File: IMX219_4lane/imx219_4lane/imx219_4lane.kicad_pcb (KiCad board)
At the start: 4 copper layers, 25 x 24 mm, 26 parts, among them J1 DF37NC-30DS-0.4V, J2 FPC 28 pin connector, Q1 NTR5103N, Q2 NTR5103N, U1 AMPM, U2 LM3670MF, U3 AP7331, U4 AP7331

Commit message: zone concept
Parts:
- moved J2 1.50 mm to (32.5, 38.8)
- moved L1 1.00 mm to (26.5, 36.0)
- moved L2 1.00 mm to (28.0, 36.0)
- moved L3 1.00 mm to (31.0, 36.0)
- moved L4 1.00 mm to (32.5, 36.0)
- moved L5 1.00 mm to (29.5, 36.0)
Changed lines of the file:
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@@
 (kicad_pcb (version 20211014) (generator pcbnew)
   (general
-    (thickness 4.69)
+    (thickness 1.60252)
   )
   (paper "A4")
@@
       (layer "F.SilkS" (type "Top Silk Screen"))
       (layer "F.Paste" (type "Top Solder Paste"))
-      (layer "F.Mask" (type "Top Solder Mask") (thickness 0.01))
-      (layer "F.Cu" (type "copper") (thickness 0.035))
-      (layer "dielectric 1" (type "core") (thickness 1.51) (material "FR4") (epsilon_r 4.5) (loss_tangent 0.02))
+      (layer "F.Mask" (type "Top Solder Mask") (thickness 0.025))
+      (layer "F.Cu" (type "copper") (thickness 0.04))
+      (layer "dielectric 1" (type "core") (thickness 0.13626) (material "FR4") (epsilon_r 4.5) (loss_tangent 0.02))
       (layer "In1.Cu" (type "copper") (thickness 0.035))
-      (layer "dielectric 2" (type "prepreg") (thickness 1.51) (material "FR4") (epsilon_r 4.5) (loss_tangent 0.02))
+      (layer "dielectric 2" (type "prepreg") (thickness 1.13) (material "FR4") (epsilon_r 4.5) (loss_tangent 0.02))
       (layer "In2.Cu" (type "copper") (thickness 0.035))
-      (layer "dielectric 3" (type "core") (thickness 1.51) (material "FR4") (epsilon_r 4.5) (loss_tangent 0.02))
-      (layer "B.Cu" (type "copper") (thickness 0.035))
-      (layer "B.Mask" (type "Bottom Solder Mask") (thickness 0.01))
+      (layer "dielectric 3" (type "core") (thickness 0.13626) (material "FR4") (epsilon_r 4.5) (loss_tangent 0.02))
+      (layer "B.Cu" (type "copper") (thickness 0.04))
+      (layer "B.Mask" (type "Bottom Solder Mask") (thickness 0.025))
       (layer "B.Paste" (type "Bottom Solder Paste"))
       (layer "B.SilkS" (type "Bottom Silk Screen"))
@@
   (net 41 "GND")
   (footprint "unsurv_offline_pcb_footprints:Molex 505110-2891" (layer "F.Cu")
-    (at 32.5 37.25)
+    (at 32.5 38.75)
     (property "Sheetfile" "imx219_4lane.kicad_sch")
     (property "Sheetname" "")
@@
     (pad "30" smd roundrect (at 9.05 2.7) (size 2 1.3) (layers "F.Cu" "F.Paste" "F.Mask") (roundrect_rratio 0.25)
       (net 2 "SHELL") (pinfunction "Pin_30") (pintype "passive"))
+    (model "${KICAD6_3DMODEL_DIR}/imported/5051102891.stp"
+      (offset (xyz 0 -1 0))
+      (scale (xyz 1 1 1))
+      (rotate (xyz -90 0 0))
+    )
   )
   (footprint "Capacitor_SMD:C_0603_1608Metric" (layer "F.Cu")
@@
   )
   (footprint "unsurv_offline_pcb_footprints:DLP11SN900HL2L_hand_solder" (layer "F.Cu")
-    (at 28 35 -90)
+    (at 28 36 -90)
     (property "Sheetfile" "imx219_4lane.kicad_sch")
     (property "Sheetname" "")
@@
     (property "Sheetname" "")
     (attr smd)
-    (fp_text reference "Q2" (at -0.475 -3.375) (layer "F.SilkS")
+    (fp_text reference "Q2" (at -0.475 -4.375) (layer "F.SilkS")
       (effects (font (size 1 1) (thickness 0.15)))
     )
@@
   )
   (footprint "unsurv_offline_pcb_footprints:DLP11SN900HL2L_hand_solder" (layer "F.Cu")
-    (at 29.5 35 -90)
+    (at 29.5 36 -90)
     (property "Sheetfile" "imx219_4lane.kicad_sch")
     (property "Sheetname" "")
@@
   )
   (footprint "unsurv_offline_pcb_footprints:DLP11SN900HL2L_hand_solder" (layer "F.Cu")
-    (at 26.5 35 90)
+    (at 26.5 36 90)
     (property "Sheetfile" "imx219_4lane.kicad_sch")
     (property "Sheetname" "")
@@
   )
   (footprint "unsurv_offline_pcb_footprints:DLP11SN900HL2L_hand_solder" (layer "F.Cu")
-    (at 31 35 -90)
+    (at 31 36 -90)
     (property "Sheetfile" "imx219_4lane.kicad_sch")
     (property "Sheetname" "")
@@
   )
   (footprint "unsurv_offline_pcb_footprints:DLP11SN900HL2L_hand_solder" (layer "F.Cu")
-    (at 32.5 35 -90)
-    (property "Sheetfile" "imx219_4lane.kicad_sch")
-    (property "Sheetname" "")
+    (at 32.5 36 -90)
+    (property "Sheetfile" "imx219_4lane.kicad_sch")
+    (property "Sheetname" "")

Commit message: update
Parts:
- moved C5 9.43 mm to (40.2, 34.6)
- moved C6 9.43 mm to (34.2, 34.6)
- moved U3 9.43 mm to (37.2, 34.6)
- moved C10 8.54 mm to (37.5, 26.0)
- moved C9 8.54 mm to (43.5, 26.0)
- moved U4 8.54 mm to (40.5, 26.0)
- moved C2 8.34 mm to (34.2, 21.2), turned to 0 degrees
- moved C1 3.75 mm to (28.2, 22.5)
- moved C3 3.72 mm to (31.0, 21.2), turned to 180 degrees
- moved Q1 2.83 mm to (23.0, 26.5)
- moved Q2 2.83 mm to (23.0, 30.0)
- moved R1 2.83 mm to (26.0, 26.5)
- moved R2 2.83 mm to (26.0, 30.0)
- moved C7 2.75 mm to (43.8, 30.0)
- moved C8 2.75 mm to (35.8, 30.0)
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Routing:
- net GND: track 0.00 -> 21.9 mm, vias 0 -> 20
- net +5V: track 0.00 -> 16.8 mm, vias 0 -> 8
- net +1V8: track 0.00 -> 4.67 mm, vias 0 -> 1
- net +1V2: track 0.00 -> 3.93 mm
- net Net-(L6-Pad2): track 0.00 -> 2.43 mm
- net +2V8: track 0.00 -> 1.93 mm
- added copper zone on In1.Cu, net +1V8
- added copper zone on In2.Cu, net +1V8
- added copper zone on In1.Cu, net +5V
- added copper zone on In2.Cu, net +5V
- added copper zone on B.Cu, net GND
- added copper zone on F.Cu, net GND

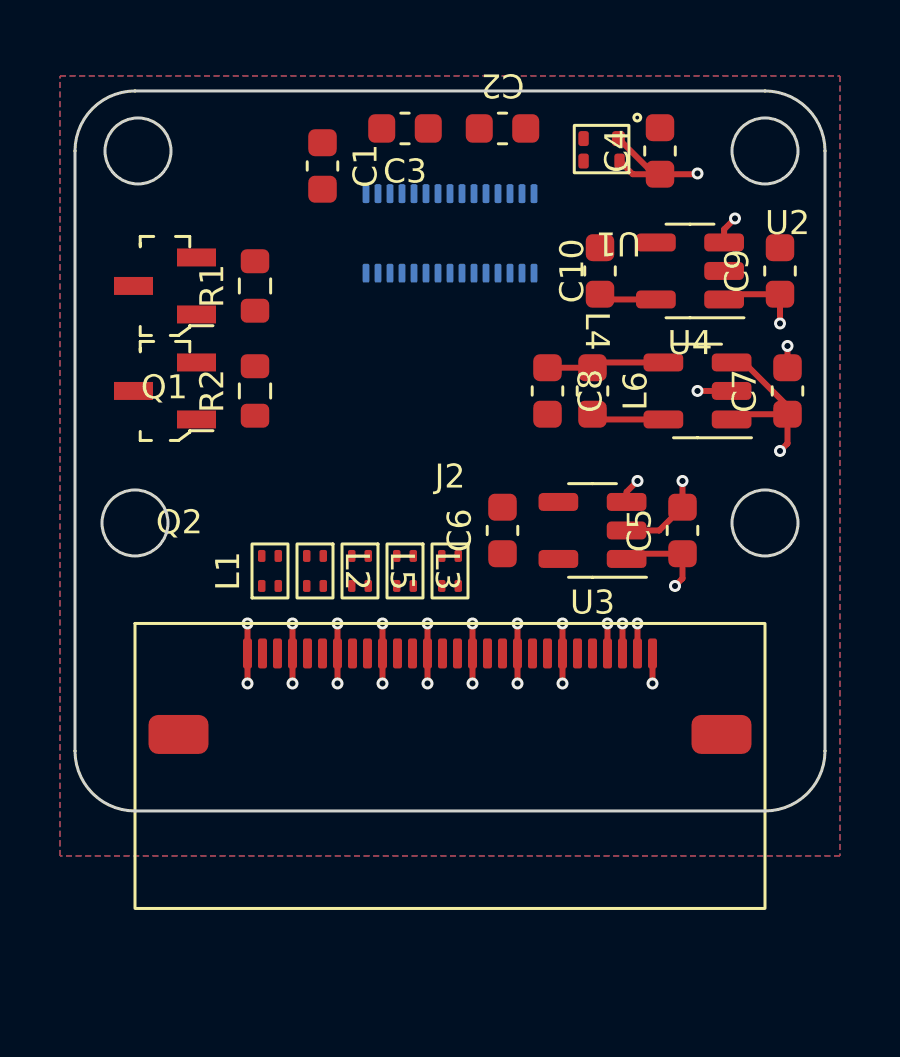
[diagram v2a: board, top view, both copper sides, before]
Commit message: added dual channel mosfet for 1v8 I2C
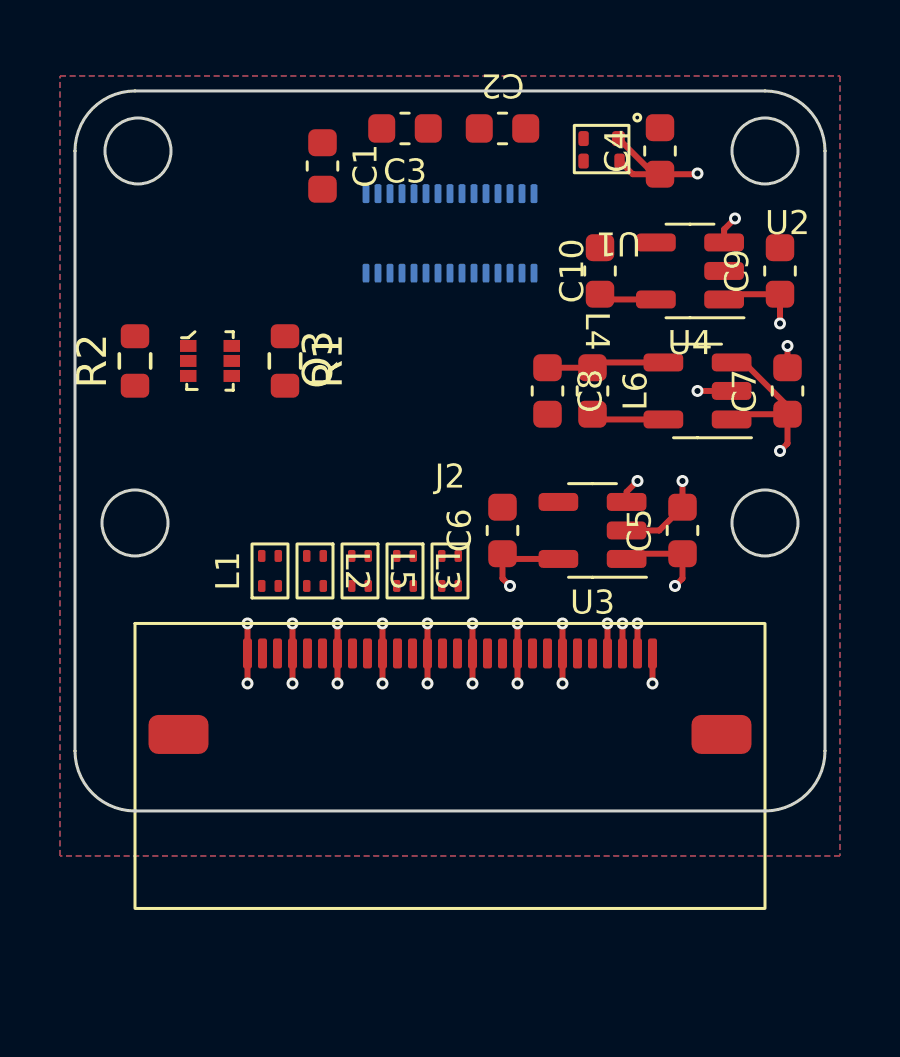
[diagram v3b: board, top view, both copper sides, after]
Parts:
- removed Q1, Q2: NTR5103N, digikey-footprints:SOT-23-3
- added Q3: NTZD3154N, digikey-footprints:SOT-563, F.Cu at (24.5, 29.0)
- moved R2 4.12 mm to (22.0, 29.0)
- moved R1 2.69 mm to (27.0, 29.0), turned to -90 degrees
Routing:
- net +1V8: track 4.67 -> 7.78 mm, vias 1 -> 2

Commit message: length matching mipi signals
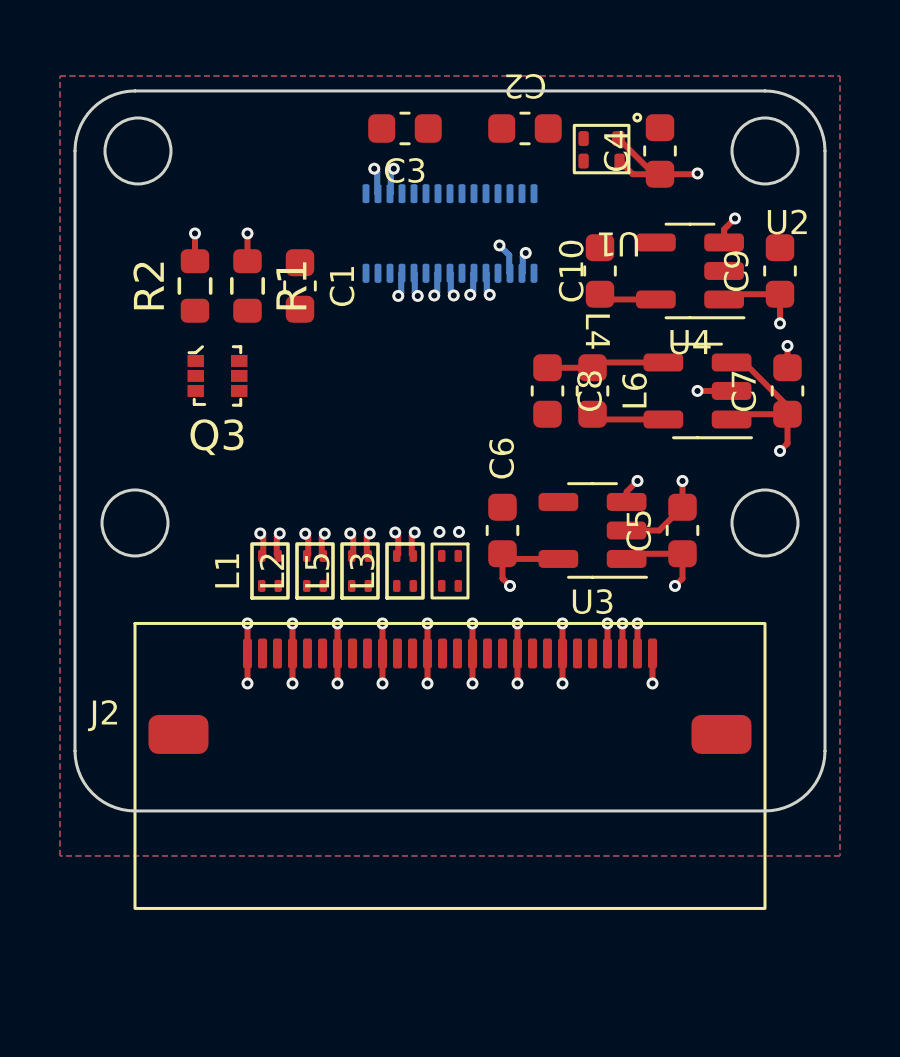
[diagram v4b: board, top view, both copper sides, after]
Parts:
- moved C1 4.07 mm to (27.5, 26.5)
- moved R2 3.20 mm to (24.0, 26.5), turned to -90 degrees
- moved R1 2.80 mm to (25.8, 26.5)
- moved C2 0.75 mm to (35.0, 21.2)
- moved Q3 0.56 mm to (24.8, 29.5)
- turned L2 to 90 degrees
- turned L3 to 90 degrees
- turned L5 to 90 degrees
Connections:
- L2 pad 1: MIPI_DATA_2_N -> MIPI_DATA_2_P
- L2 pad 2: CSI_D2N -> CSI_D2P
- L2 pad 3: CSI_D2P -> CSI_D2N
- L2 pad 4: MIPI_DATA_2_P -> MIPI_DATA_2_N
- L3 pad 1: MIPI_DATA_1_N -> MIPI_DATA_1_P
- L3 pad 2: CSI_D1N -> CSI_D1P
- L3 pad 3: CSI_D1P -> CSI_D1N
- L3 pad 4: MIPI_DATA_1_P -> MIPI_DATA_1_N
- L5 pad 1: MIPI_CLK_N -> MIPI_CLK_P
- L5 pad 2: CSI_CLKN -> CSI_CLKP
- L5 pad 3: CSI_CLKP -> CSI_CLKN
- L5 pad 4: MIPI_CLK_P -> MIPI_CLK_N
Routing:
- net CSI_D0N: track 0.00 -> 20.5 mm, vias 0 -> 2
- net CSI_D0P: track 0.00 -> 20.4 mm, vias 0 -> 2
- net CSI_D2P: track 0.00 -> 19.3 mm, vias 0 -> 2
- net CSI_D3P: track 0.00 -> 17.9 mm, vias 0 -> 2
- net CSI_D1N: track 0.00 -> 16.4 mm, vias 0 -> 2
- net CSI_D1P: track 0.00 -> 16.3 mm, vias 0 -> 2
- net CSI_CLKP: track 0.00 -> 16.3 mm, vias 0 -> 2
- net CSI_D3N: track 0.00 -> 16.3 mm, vias 0 -> 2
- net CSI_D2N: track 0.00 -> 16.3 mm, vias 0 -> 2
- net CSI_CLKN: track 0.00 -> 16.3 mm, vias 0 -> 2
- net (no net): track 0.00 -> 7.83 mm
- net +1V8: track 7.78 -> 9.63 mm, vias 2 -> 4

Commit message: prototype routing
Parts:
- moved C1 1.89 mm to (28.5, 24.9), turned to 90 degrees
- moved Q3 1.51 mm to (24.6, 31.0)
- turned L4 to 90 degrees
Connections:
- L4 pad 1: MIPI_DATA_0_N -> MIPI_DATA_0_P
- L4 pad 2: CSI_D0N -> CSI_D0P
- L4 pad 3: CSI_D0P -> CSI_D0N
- L4 pad 4: MIPI_DATA_0_P -> MIPI_DATA_0_N
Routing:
- net I2C_SDA_3V3: track 0.00 -> 22.6 mm, vias 0 -> 2
- net I2C_SCL_3V3: track 0.00 -> 22.5 mm, vias 0 -> 2
- net +1V8: track 9.63 -> 21.5 mm, vias 4 -> 8
- net +2V8: track 1.93 -> 13.6 mm, vias 0 -> 2
- net SCL_1V8: track 0.00 -> 11.4 mm, vias 0 -> 1
- net +1V2: track 3.93 -> 14.2 mm, vias 0 -> 1
- net SDA_1V8: track 0.00 -> 10.1 mm, vias 0 -> 1
- net (no net): track 7.83 -> 15.7 mm
- net GND: track 21.9 -> 28.9 mm, vias 20 -> 29
- net MCLK: track 0.00 -> 6.96 mm, vias 0 -> 1
- net CSI_D0P: track 20.4 -> 22.8 mm
- net CSI_D0N: track 20.5 -> 22.8 mm
- net MIPI_DATA_3_P: track 0.00 -> 2.26 mm
- net MIPI_DATA_3_N: track 0.00 -> 2.26 mm
- net MIPI_DATA_2_P: track 0.00 -> 2.26 mm
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
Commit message: flip connector -.-
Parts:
- added TP1: TestPoint, unsurv_offline_pcb_footprints:TestPoint_Pad_D0.7mm, F.Cu at (22.0, 28.6)
- added TP2: TestPoint, unsurv_offline_pcb_footprints:TestPoint_Pad_D0.7mm, F.Cu at (34.5, 27.9)
- added TP3: TestPoint, unsurv_offline_pcb_footprints:TestPoint_Pad_D0.7mm, F.Cu at (22.0, 30.6)
- added TP4: TestPoint, unsurv_offline_pcb_footprints:TestPoint_Pad_D0.7mm, F.Cu at (26.2, 32.7)
- added TP5: TestPoint, unsurv_offline_pcb_footprints:TestPoint_Pad_D0.7mm, F.Cu at (22.0, 26.8)
- added TP6: TestPoint, unsurv_offline_pcb_footprints:TestPoint_Pad_D0.7mm, F.Cu at (37.9, 23.6)
- moved J2 4.50 mm to (32.5, 43.2), turned to 180 degrees
- moved C5 1.11 mm to (40.4, 33.5)
- moved C6 1.11 mm to (34.4, 33.5)
- moved U3 1.11 mm to (37.4, 33.5)
- moved C9 0.56 mm to (43.8, 26.5)
- moved C7 0.45 mm to (43.8, 29.6)
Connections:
- J2 pad 11: MIPI_DATA_1_P -> SAI2_TXC
- J2 pad 12: MIPI_DATA_1_N -> SAI2_TXFS
- J2 pad 14: MIPI_DATA_0_P -> MIPI_DATA_0_N
- J2 pad 15: MIPI_DATA_0_N -> MIPI_DATA_0_P
- J2 pad 17: SAI2_TXFS -> MIPI_DATA_1_N
- J2 pad 18: SAI2_TXC -> MIPI_DATA_1_P
- J2 pad 2: MIPI_DATA_3_P -> +5V
- J2 pad 20: I2C_SCL_3V3 -> MIPI_CLK_N
- J2 pad 21: I2C_SDA_3V3 -> MIPI_CLK_P
- J2 pad 23: SAI2_RXD0 -> MIPI_DATA_2_N
- J2 pad 24: SAI2_TXD0 -> MIPI_DATA_2_P
- J2 pad 25: +5V -> GND
- J2 pad 26: +5V -> MIPI_DATA_3_N
- J2 pad 27: +5V -> MIPI_DATA_3_P
- J2 pad 3: MIPI_DATA_3_N -> +5V
- J2 pad 4: GND -> +5V
- J2 pad 5: MIPI_DATA_2_P -> SAI2_TXD0
- J2 pad 6: MIPI_DATA_2_N -> SAI2_RXD0
- J2 pad 8: MIPI_CLK_P -> I2C_SDA_3V3
- J2 pad 9: MIPI_CLK_N -> I2C_SCL_3V3
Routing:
- net MIPI_DATA_2_P: track 2.26 -> 6.80 mm
- net MIPI_DATA_1_P: track 2.26 -> 6.80 mm
- net MIPI_DATA_1_N: track 2.26 -> 6.80 mm
- net MIPI_CLK_N: track 2.26 -> 6.80 mm
- net MIPI_DATA_3_P: track 2.26 -> 6.76 mm
- net MIPI_DATA_3_N: track 2.26 -> 6.76 mm
- net MIPI_DATA_2_N: track 2.26 -> 6.76 mm
- net MIPI_DATA_0_P: track 2.26 -> 6.76 mm
- net MIPI_DATA_0_N: track 2.26 -> 6.76 mm
- net MIPI_CLK_P: track 2.26 -> 6.76 mm
- net GND: track 28.9 -> 24.6 mm, vias 29 -> 52
- net +5V: track 16.8 -> 19.3 mm
- net +1V2: track 14.2 -> 16.1 mm
- net SDA_1V8: track 10.1 -> 11.9 mm
- net SCL_1V8: track 11.4 -> 13.0 mm
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
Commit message: fix 1V2 layout
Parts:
- moved C4 14.7 mm to (24.8, 21.7), turned to -90 degrees
- moved U1 11.9 mm to (26.2, 22.1), turned to 0 degrees
- moved TP6 9.67 mm to (28.6, 21.0), turned to 180 degrees
- moved C7 8.28 mm to (39.1, 22.7), turned to 0 degrees
- moved L6 8.17 mm to (44.0, 25.4), turned to 90 degrees
- moved U2 4.66 mm to (41.1, 25.4), turned to 0 degrees
- moved C8 4.19 mm to (38.2, 26.6), turned to 90 degrees
- moved C10 3.90 mm to (36.9, 29.9)
- moved C9 3.90 mm to (43.1, 30.4)
- moved U4 3.90 mm to (39.9, 29.9)
- moved TP2 2.20 mm to (36.7, 27.4)
- moved C6 1.53 mm to (33.9, 32.1)
- moved C5 0.64 mm to (39.8, 33.5)
- moved U3 0.64 mm to (36.8, 33.5)
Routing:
- net +1V2: track 16.1 -> 20.1 mm
- net +2V8: track 13.6 -> 17.0 mm
- net +5V: track 19.3 -> 21.3 mm, vias 8 -> 9
- net GND: track 24.6 -> 25.4 mm, vias 52 -> 68
- net Net-(L6-Pad2): track 2.43 -> 1.86 mm
